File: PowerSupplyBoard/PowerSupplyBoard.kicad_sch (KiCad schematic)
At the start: 8 parts, among them J1 power input, J2 to inverter PCB

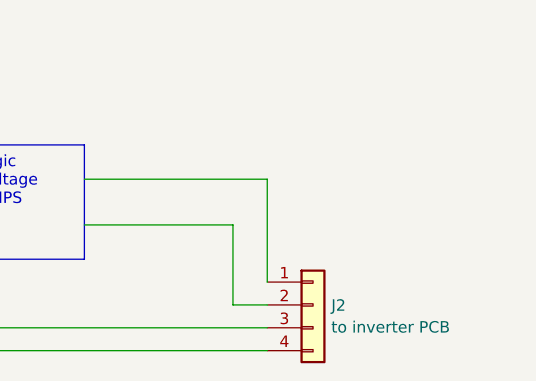
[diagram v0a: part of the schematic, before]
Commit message: Documenting internal power connector
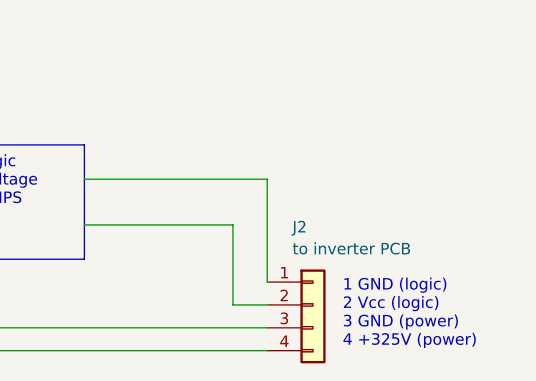
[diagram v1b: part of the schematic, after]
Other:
- note added: "1 GND (logic) 2 Vcc (logic) 3 GND (power) 4 +325V (power)"
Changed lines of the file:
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@@
+		)
+	)
+	(text "1 GND (logic)\n2 Vcc (logic)\n3 GND (power)\n4 +325V (power)\n"
+		(exclude_from_sim no)
+		(at 231.902 120.396 0)
+		(effects
+			(font
+				(size 1.27 1.27)
+			)
+			(justify left)
 		)
 	)
@@
 		(on_board yes)
 		(dnp no)
-		(fields_autoplaced yes)
 		(property "Reference" "J2"
-			(at 230.632 119.4378 0)
+			(at 226.314 110.744 0)
 			(effects
 				(font
@@
 		)
 		(property "Value" "to inverter PCB"
-			(at 230.632 121.8621 0)
+			(at 226.314 113.1683 0)
 			(effects
 				(font
